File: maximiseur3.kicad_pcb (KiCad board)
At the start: 2 copper layers, 150 x 100 mm, 41 parts, among them J1 PV+/M+, J2 M-, J3 PV-, P1 SW SW, Q1 IRLB3036G, Q2 IRLB3036G, Q3 IRLB3036G, Q4 IRLB3036G, T1 BD139, U1 LM311

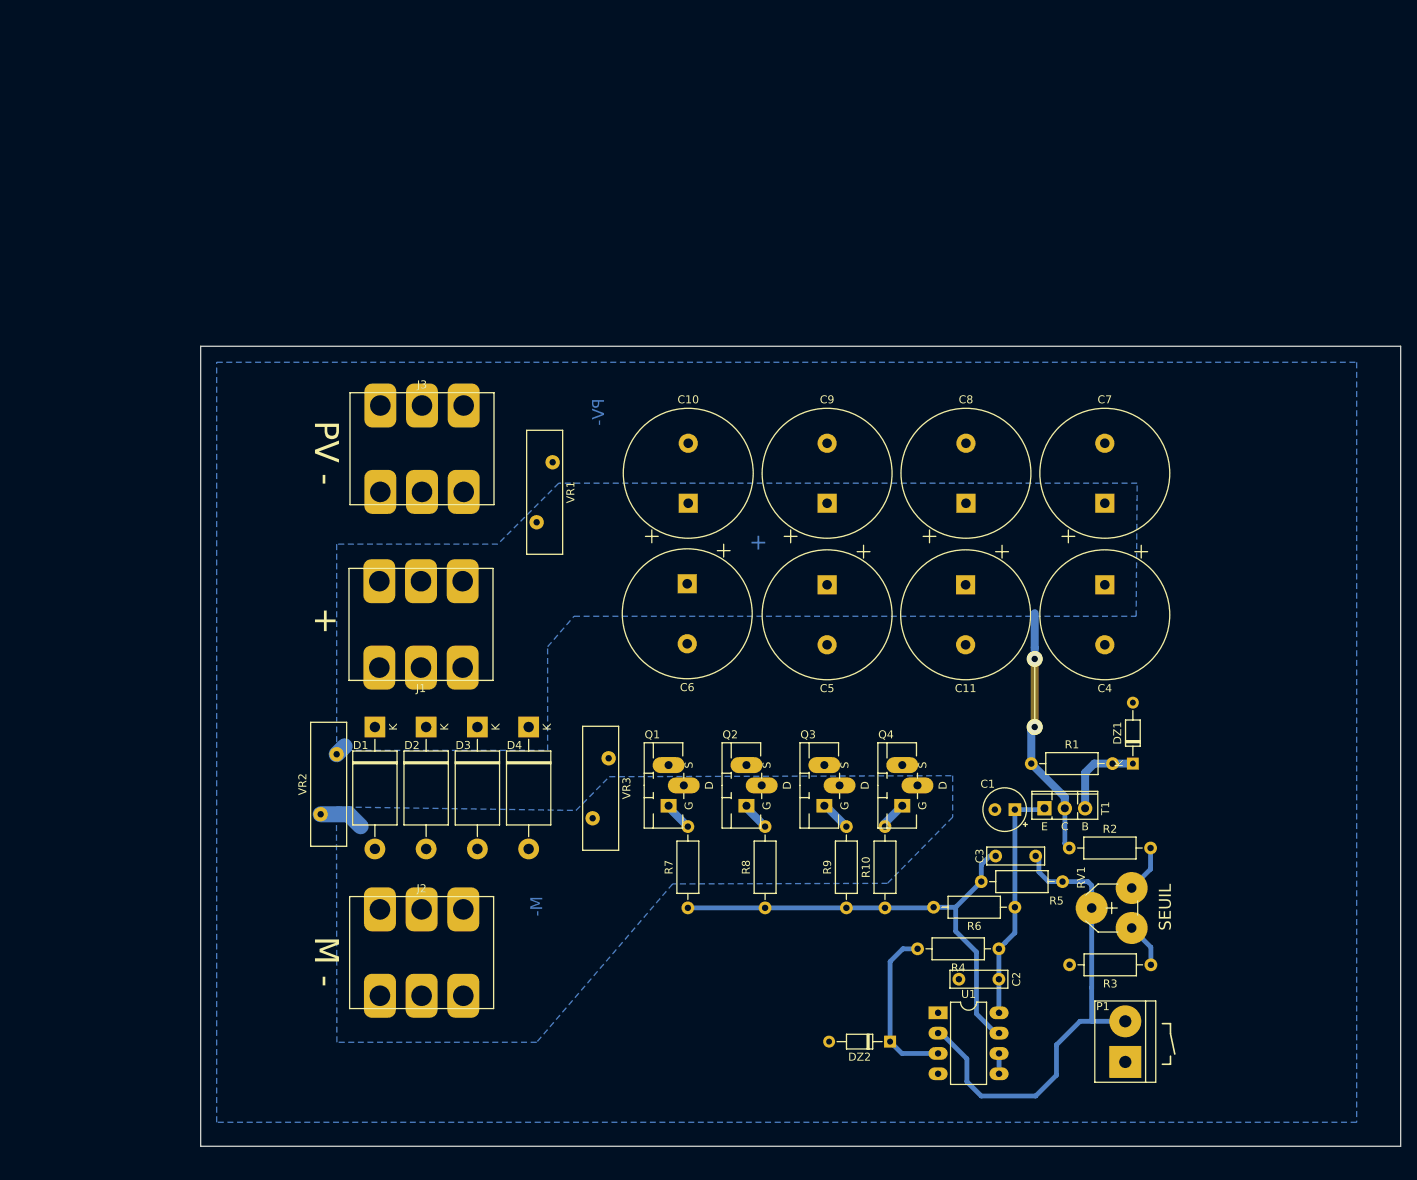
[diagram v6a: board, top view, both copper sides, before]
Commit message: modification PCB : trous de fixation + un peu de ménage
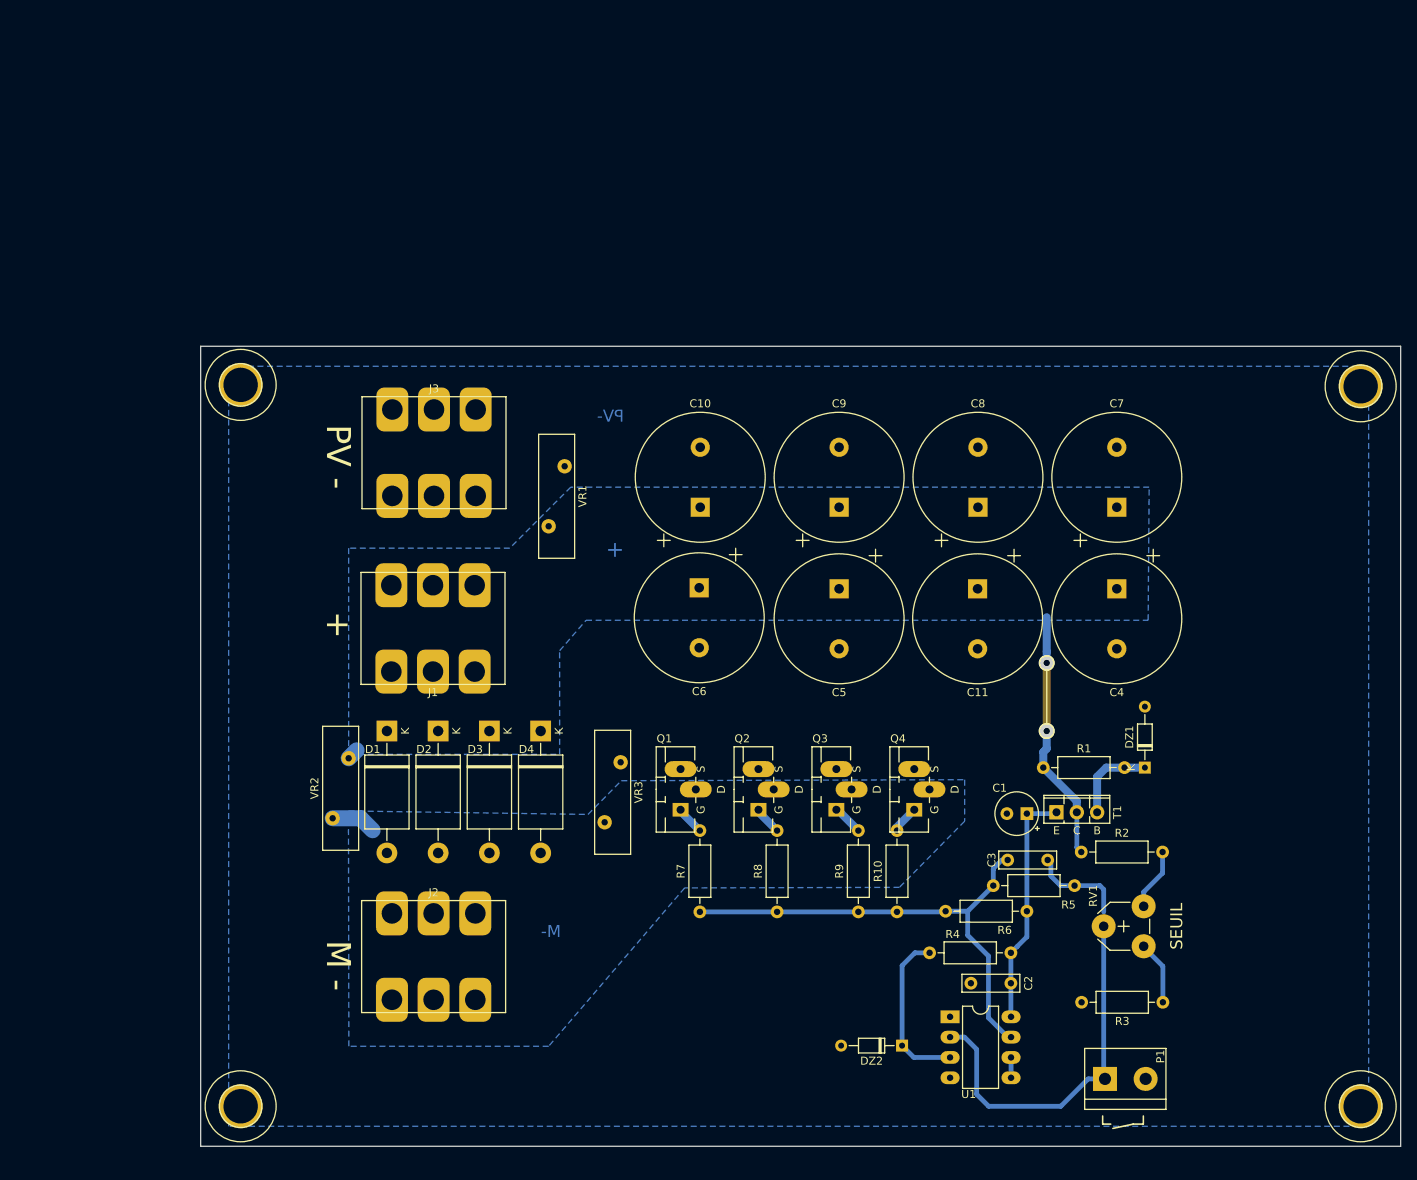
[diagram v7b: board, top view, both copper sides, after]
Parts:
- added H1: MountingHole, maximiseur:MountingHole_4.3mm_M4, F.Cu at (41.6, 39.4)
- added H2: MountingHole, maximiseur:MountingHole_4.3mm_M4, F.Cu at (41.6, 129.5)
- added H3: MountingHole, maximiseur:MountingHole_4.3mm_M4, F.Cu at (181.6, 39.5)
- added H4: MountingHole, maximiseur:MountingHole_4.3mm_M4, F.Cu at (181.6, 129.5)
- moved R3 4.92 mm to (156.9, 116.5)
- moved P1 4.66 mm to (152.2, 126.1), turned to 0 degrees
- moved RV1 2.73 mm to (154.5, 109.5)
- moved C1 1.58 mm to (139.9, 93.0)
- moved C10 1.58 mm to (99.0, 54.7)
- moved C11 1.58 mm to (133.7, 64.9)
- moved C2 1.58 mm to (137.9, 114.2)
- moved C3 1.58 mm to (137.5, 98.8)
- moved C4 1.58 mm to (151.1, 64.9)
- moved C5 1.58 mm to (116.4, 64.9)
- moved C6 1.58 mm to (98.9, 64.7)
- moved C7 1.58 mm to (151.1, 54.7)
- moved C8 1.58 mm to (133.7, 54.7)
- moved C9 1.58 mm to (116.4, 54.7)
- moved D1 1.58 mm to (59.9, 82.6)
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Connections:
- P1 pad 1: /PV- -> /RC
- P1 pad 2: /RC -> /PV-
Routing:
- net Net-(R3-Pad1): track 5.60 -> 7.89 mm
- net /RC: track 60.7 -> 58.9 mm
- net Net-(R2-Pad2): track 5.98 -> 7.76 mm

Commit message: derniers ajustements sur serigraphie avant export
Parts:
- C1: footprint Capacitor_THT:CP_Radial_D5.0mm_P2.50mm -> maximiseur:CP_Radial_D5.0mm_P2.50mm
- C2, C3: footprint Capacitor_THT:C_Rect_L7.0mm_W2.0mm_P5.00mm -> maximiseur:C_Rect_L7.0mm_W2.0mm_P5.00mm
- DZ1: value 15V -> 12V; footprint Diode_THT:D_DO-34_SOD68_P7.62mm_Horizontal -> maximiseur:D_DO-34_SOD68_P7.62mm_Horizontal
- DZ2: footprint Diode_THT:D_DO-34_SOD68_P7.62mm_Horizontal -> maximiseur:D_DO-34_SOD68_P7.62mm_Horizontal
- R1, R10, R2, R3, R4, R5, R6, R7, R8, R9: footprint Resistor_THT:R_Axial_DIN0207_L6.3mm_D2.5mm_P10.16mm_Horizontal -> maximiseur:R_Axial_DIN0207_L6.3mm_D2.5mm_P10.16mm_Horizontal
- T1: footprint Package_TO_SOT_THT:TO-126-3_Vertical -> maximiseur:TO-126-3_Vertical
- U1: footprint Package_DIP:DIP-8_W7.62mm_LongPads -> maximiseur:DIP-8_W7.62mm_LongPads
- VR1, VR2, VR3: footprint Varistor:RV_Disc_D15.5mm_W4.5mm_P7.5mm -> maximiseur:RV_Disc_D15.5mm_W4.5mm_P7.5mm
- moved C4 52.1 mm to (99.0, 64.9)
- moved C11 36.2 mm to (99.0, 54.7), turned to 90 degrees
- moved C6 34.9 mm to (133.8, 64.9)
- moved C8 17.4 mm to (151.1, 54.7)
- moved C9 17.4 mm to (133.8, 54.7)
- moved C10 17.3 mm to (116.4, 54.7)
- moved C7 10.2 mm to (151.1, 64.9), turned to 270 degrees
